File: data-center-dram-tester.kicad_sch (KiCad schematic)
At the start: 2 parts

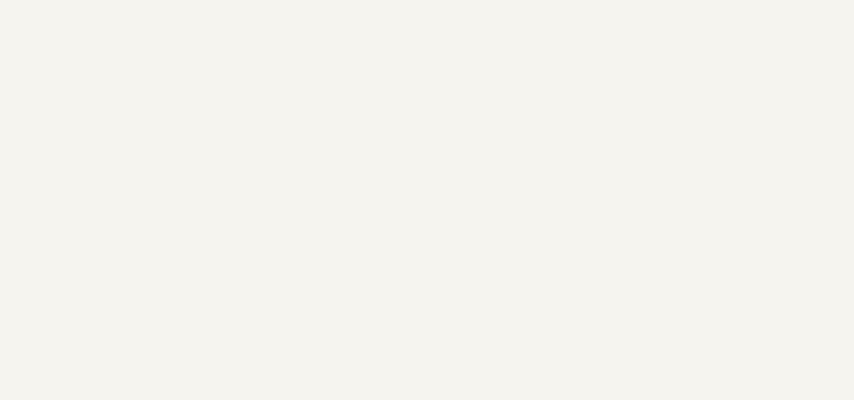
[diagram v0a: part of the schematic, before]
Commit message: Re-add mounting holes, add tri-state buffer for FPGA_POWER_CYCLE signal
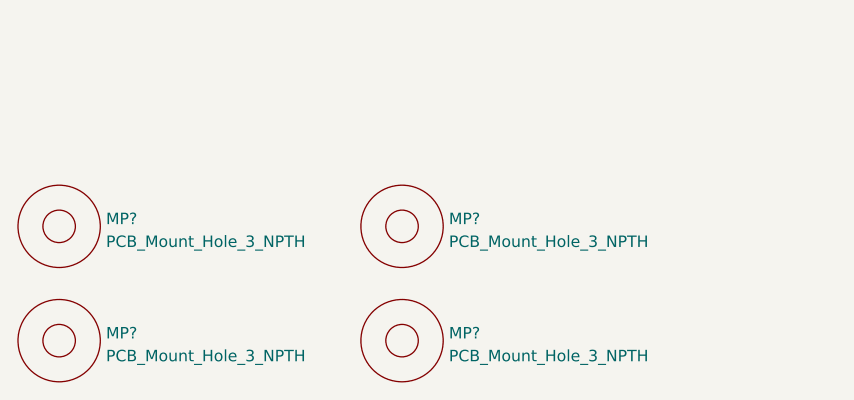
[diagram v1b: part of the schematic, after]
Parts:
- added MP? (x4): PCB_Mount_Hole_3_NPTH, antmicro-footprints:mounting-hole-3mm-NPTH, symbol antmicroMechanicalParts:PCB_Mount_Hole_3_NPTH
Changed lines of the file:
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@@
+    )
+  )
+  (symbol (lib_id "antmicroMechanicalParts:PCB_Mount_Hole_3_NPTH") (at 88.9 279.4 0) (unit 1)
+    (in_bom yes) (on_board yes) (fields_autoplaced)
+    (property "Reference" "MP?" (id 0) (at 94.107 278.5653 0)
+      (effects (font (size 1.27 1.27)) (justify left))
+    )
+    (property "Value" "PCB_Mount_Hole_3_NPTH" (id 1) (at 94.107 281.1022 0)
+      (effects (font (size 1.27 1.27)) (justify left))
+    )
+    (property "Footprint" "antmicro-footprints:mounting-hole-3mm-NPTH" (id 2) (at 109.22 261.62 0)
+      (effects (font (size 1.27 1.27)) hide)
+    )
+    (property "Datasheet" "" (id 3) (at 113.03 259.08 0)
+      (effects (font (size 1.27 1.27)) hide)
+    )
+  )
+  (symbol (lib_id "antmicroMechanicalParts:PCB_Mount_Hole_3_NPTH") (at 88.9 266.7 0) (unit 1)
+    (in_bom yes) (on_board yes) (fields_autoplaced)
+    (property "Reference" "MP?" (id 0) (at 94.107 265.8653 0)
+      (effects (font (size 1.27 1.27)) (justify left))
+    )
+    (property "Value" "PCB_Mount_Hole_3_NPTH" (id 1) (at 94.107 268.4022 0)
+      (effects (font (size 1.27 1.27)) (justify left))
+    )
+    (property "Footprint" "antmicro-footprints:mounting-hole-3mm-NPTH" (id 2) (at 109.22 248.92 0)
+      (effects (font (size 1.27 1.27)) hide)
+    )
+    (property "Datasheet" "" (id 3) (at 113.03 246.38 0)
+      (effects (font (size 1.27 1.27)) hide)
+    )
+  )
+  (symbol (lib_id "antmicroMechanicalParts:PCB_Mount_Hole_3_NPTH") (at 127 279.4 0) (unit 1)
+    (in_bom yes) (on_board yes) (fields_autoplaced)
+    (property "Reference" "MP?" (id 0) (at 132.207 278.5653 0)
+      (effects (font (size 1.27 1.27)) (justify left))
+    )
+    (property "Value" "PCB_Mount_Hole_3_NPTH" (id 1) (at 132.207 281.1022 0)
+      (effects (font (size 1.27 1.27)) (justify left))
+    )
+    (property "Footprint" "antmicro-footprints:mounting-hole-3mm-NPTH" (id 2) (at 147.32 261.62 0)
+      (effects (font (size 1.27 1.27)) hide)
+    )
+    (property "Datasheet" "" (id 3) (at 151.13 259.08 0)
+      (effects (font (size 1.27 1.27)) hide)
+    )
+  )
+  (symbol (lib_id "antmicroMechanicalParts:PCB_Mount_Hole_3_NPTH") (at 127 266.7 0) (unit 1)
+    (in_bom yes) (on_board yes) (fields_autoplaced)
+    (property "Reference" "MP?" (id 0) (at 132.207 265.8653 0)
+      (effects (font (size 1.27 1.27)) (justify left))
+    )
+    (property "Value" "PCB_Mount_Hole_3_NPTH" (id 1) (at 132.207 268.4022 0)
+      (effects (font (size 1.27 1.27)) (justify left))
+    )
+    (property "Footprint" "antmicro-footprints:mounting-hole-3mm-NPTH" (id 2) (at 147.32 248.92 0)
+      (effects (font (size 1.27 1.27)) hide)
+    )
+    (property "Datasheet" "" (id 3) (at 151.13 246.38 0)
+      (effects (font (size 1.27 1.27)) hide)
     )
   )
@@
       (reference "#PWR?") (unit 1) (value "GND") (footprint "")
     )
+    (path "/00000000-0000-0000-0000-000060225b0c/680d5635-2fe8-4c65-b69d-3a0ebe167ce5"
+      (reference "#PWR?") (unit 1) (value "GND") (footprint "")
+    )
     (path "/00000000-0000-0000-0000-000060225b0c/704407d4-b28e-4ba5-a5ae-3afafb967f7d"
       (reference "#PWR?") (unit 1) (value "GND") (footprint "")
@@
       (reference "#PWR?") (unit 1) (value "GND") (footprint "")
     )
+    (path "/00000000-0000-0000-0000-000060225b0c/baa345af-9976-450b-b058-62742e508d67"
+      (reference "#PWR?") (unit 1) (value "GND") (footprint "")
+    )
     (path "/00000000-0000-0000-0000-000060225b0c/f422fc8e-06b8-4d01-b49c-7a4d75f384b9"
       (reference "#PWR?") (unit 1) (value "GND") (footprint "")
@@
       (reference "C274") (unit 1) (value "C_100n_0402") (footprint "antmicro-footprints:0402-cap")
     )
+    (path "/00000000-0000-0000-0000-000060225b0c/1cb35a3d-f090-4897-872e-c417376c89e8"
+      (reference "C?") (unit 1) (value "C_100n_0402") (footprint "antmicro-footprints:0402-cap")
+    )
     (path "/00000000-0000-0000-0000-000060225b0c/844f41a4-4874-4397-b068-4b2e421400a8"
       (reference "C?") (unit 1) (value "C_100n_0402") (footprint "antmicro-footprints:0402-cap")
@@
       (reference "L7") (unit 1) (value "SRP0420-1R5K") (footprint "data-center-dram-tester-footprints:SRP4020")
     )
+    (path "/4d7ac6a2-6294-4556-983c-5446f8c4f7ea"
+      (reference "MP?") (unit 1) (value "PCB_Mount_Hole_3_NPTH") (footprint "antmicro-footprints:mounting-hole-3mm-NPTH")
+    )
+    (path "/6ad09738-5d12-4303-b619-634d240a9a3f"
+      (reference "MP?") (unit 1) (value "PCB_Mount_Hole_3_NPTH") (footprint "antmicro-footprints:mounting-hole-3mm-NPTH")
+    )
+    (path "/a11342d1-c811-4475-a80f-8e2553b31c01"
+      (reference "MP?") (unit 1) (value "PCB_Mount_Hole_3_NPTH") (footprint "antmicro-footprints:mounting-hole-3mm-NPTH")
+    )
+    (path "/a4a8edea-3b3f-48a5-b30a-9a448d5392f1"
+      (reference "MP?") (unit 1) (value "PCB_Mount_Hole_3_NPTH") (footprint "antmicro-footprints:mounting-hole-3mm-NPTH")
+    )
     (path "/00000000-0000-0000-0000-0000603b54ea"
       (reference "N1") (unit 1) (value "oshw_logo") (footprint "data-center-dram-tester-footprints:oshw-logo")
@@
       (reference "U?") (unit 1) (value "SN74LVC1G125DBVR") (footprint "antmicro-footprints:SOT-753")
     )
+    (path "/00000000-0000-0000-0000-000060225b0c/19de246d-795d-4557-ab13-30034afacff0"
+      (reference "U?") (unit 1) (value "SN74LVC1G125DBVR") (footprint "antmicro-footprints:SOT-753")
+    )

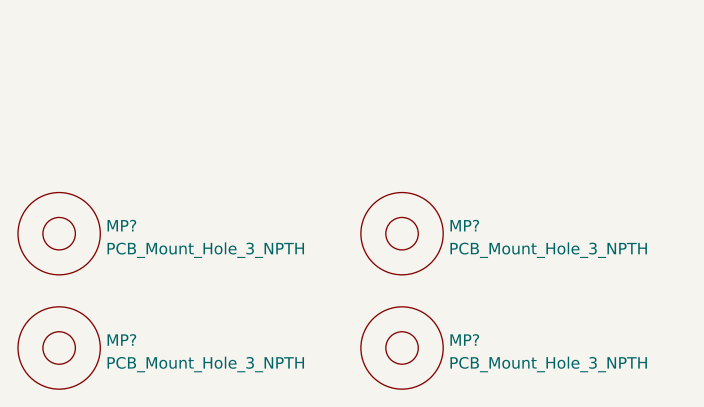
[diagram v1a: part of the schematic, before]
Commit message: Correct PCIe pin assigment, replace MODE2 symbol, export changes to PCB, progess in the new components placement
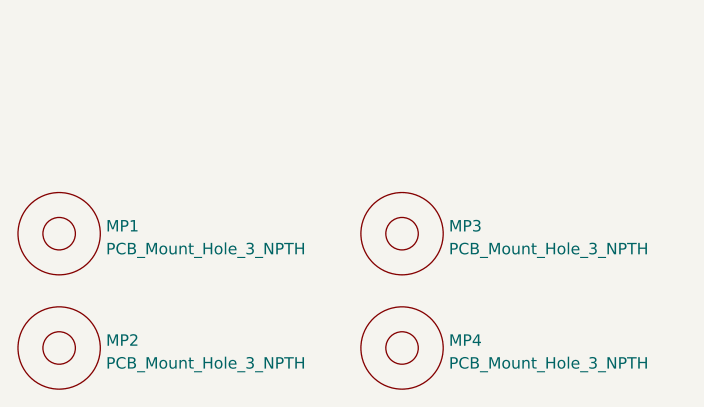
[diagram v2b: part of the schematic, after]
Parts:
- gave numbers to parts that had none: 4
